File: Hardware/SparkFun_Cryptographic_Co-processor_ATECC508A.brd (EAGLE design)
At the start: 25.4 x 25.4 mm, 41 parts, among them J1 QWIIC, J2 QWIIC, J3 PTH, U1 ATECC508A

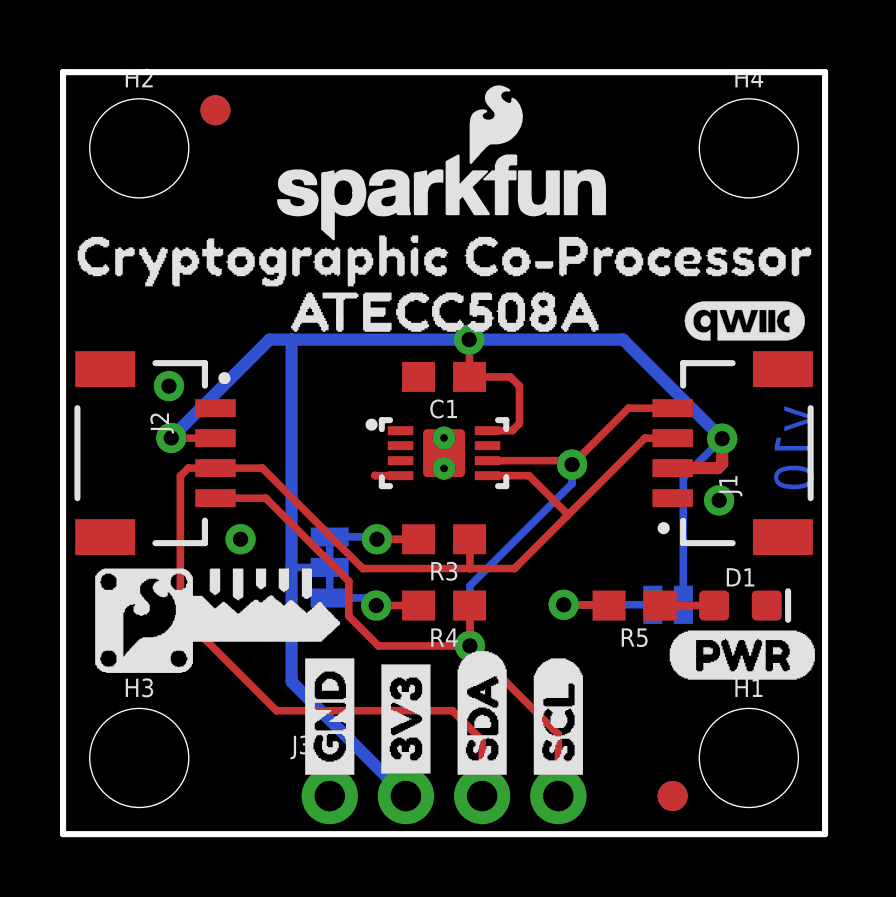
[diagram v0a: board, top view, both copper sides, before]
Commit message: swapped over to official SFE library for IC
added name and value to footprint.
removed local mini library.
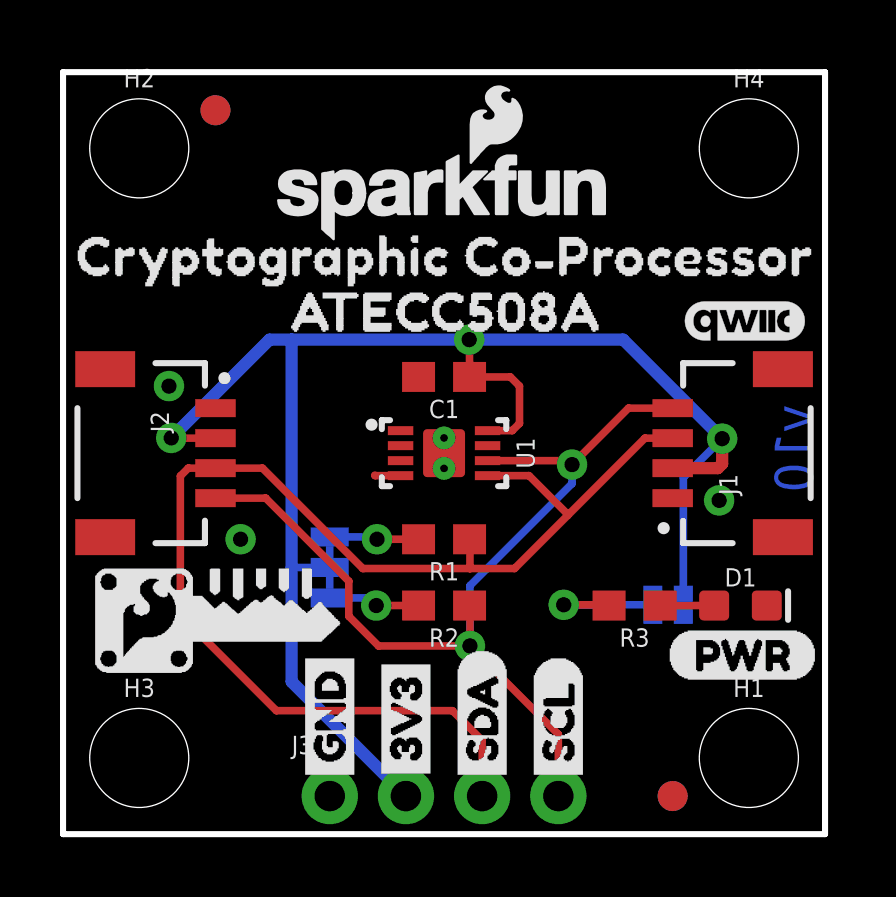
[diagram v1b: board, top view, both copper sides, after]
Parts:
- removed R5: 1k, SparkFun-Resistors:0603
- added R1: 4.7k, SparkFun-Resistors:0603
- R3: value 4.7k -> 1k
- U1: device ATECC508A:UDFN_2X3MM -> SparkFun-IC-Special-Function:UDFN_2X3MM
- moved R3 6.72 mm to (19.1, 7.62)
- renumbered R4 to R2
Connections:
- net N$3: now also R3.1; no longer R5.1
- net N$4: now also R1.2; no longer R3.2
- net N$7: now also R3.2; no longer R5.2
- net SDA: now also R1.1; no longer R3.1
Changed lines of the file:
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@@
 <attribute name="REV" value="" x="-13.97" y="-12.7" size="1.778" layer="27" display="off"/>
 </element>
-<element name="R3" library="SparkFun-Resistors" package="0603" value="4.7k" x="12.7" y="9.8298" smashed="yes" rot="R180">
+<element name="R1" library="SparkFun-Resistors" package="0603" value="4.7k" x="12.7" y="9.8298" smashed="yes" rot="R180">
 <attribute name="NAME" x="12.7" y="9.0678" size="0.6096" layer="25" font="vector" ratio="20" rot="R180" align="bottom-center"/>
 <attribute name="PROD_ID" value="RES-07857" x="12.7" y="9.8298" size="1.778" layer="27" font="vector" ratio="15" rot="R180" display="off"/>
 <attribute name="VALUE" x="12.7" y="10.5918" size="0.6096" layer="27" font="vector" ratio="20" rot="R180" align="top-center"/>
 </element>
-<element name="R4" library="SparkFun-Resistors" package="0603" value="4.7k" x="12.7" y="7.62" smashed="yes" rot="R180">
+<element name="R2" library="SparkFun-Resistors" package="0603" value="4.7k" x="12.7" y="7.62" smashed="yes" rot="R180">
 <attribute name="NAME" x="12.7" y="6.858" size="0.6096" layer="25" font="vector" ratio="20" rot="R180" align="bottom-center"/>
 <attribute name="PROD_ID" value="RES-07857" x="12.7" y="7.62" size="1.778" layer="27" font="vector" ratio="15" rot="R180" display="off"/>
@@
 <attribute name="VALUE" x="22.5806" y="6.985" size="0.6096" layer="27" font="vector" ratio="20" align="top-center"/>
 </element>
-<element name="R5" library="SparkFun-Resistors" package="0603" value="1k" x="19.05" y="7.62" smashed="yes" rot="R180">
+<element name="R3" library="SparkFun-Resistors" package="0603" value="1k" x="19.05" y="7.62" smashed="yes" rot="R180">
 <attribute name="NAME" x="19.05" y="6.858" size="0.6096" layer="25" font="vector" ratio="20" rot="R180" align="bottom-center"/>
 <attribute name="PROD_ID" value="RES-07856" x="19.05" y="7.62" size="1.778" layer="27" font="vector" ratio="15" rot="R180" display="off"/>
@@
 <attribute name="VALUE" x="2.54" y="0.508" size="0.6096" layer="27" font="vector" ratio="20" align="top-center"/>
 </element>
-<element name="U1" library="ATECC508A" package="UDFN_2X3MM" value="ATECC508A" x="12.7" y="12.7" smashed="yes" rot="R270">
-<attribute name="PROD_ID" value="IC-14661" x="12.7" y="12.7" size="1.778" layer="27" rot="R270" display="off"/>
-</element>
 <element name="U$17" library="buzzard_labels (5)" package="CRYPTOGRAPHIC_CO#PROCESSOR0" value="" x="-0.7112" y="19.2786" smashed="yes"/>
 <element name="U$12" library="buzzard_labels (7)" package="ATECC508A0" value="" x="6.4008" y="17.4244" smashed="yes"/>
@@
 <element name="U$15" library="crypto_coprocessor_logo#04#png (1)" package="CRYPTO_COPROCESSOR_LOGO#04#PNG" value="" x="12.7" y="13.97" smashed="yes" rot="MR0"/>
 <element name="U$18" library="crypto_coprocessor_logo#04#png (2)" package="CRYPTO_COPROCESSOR_LOGO#04#PNG" value="" x="5.08" y="7.2136" smashed="yes"/>
+<element name="U1" library="SparkFun-IC-Special-Function" package="UDFN_2X3MM" value="ATECC508A" x="12.7" y="12.7" smashed="yes" rot="R270">
+<attribute name="NAME" x="15.113" y="12.7" size="0.6096" layer="25" font="vector" ratio="20" rot="R270" align="bottom-center"/>
+<attribute name="PROD_ID" value="IC-14661" x="12.7" y="12.7" size="1.778" layer="27" rot="R270" display="off"/>
+<attribute name="VALUE" x="9.906" y="12.7" size="0.6096" layer="27" font="vector" ratio="20" rot="R90" align="bottom-center"/>
+</element>
 </elements>
 <signals>
@@
 <contactref element="C1" pad="2"/>
 <contactref element="D1" pad="C"/>
-<contactref element="U1" pad="4"/>
-<contactref element="U1" pad="P"/>
 <wire x1="12.7" y1="12.7" x2="12.7706" y2="12.6294" width="0.254" layer="1"/>
 <wire x1="12.7" y1="12.7" x2="12.6294" y2="12.6294" width="0.254" layer="1"/>
@@
 <wire x1="10.402" y1="11.95" x2="10.3886" y2="11.9634" width="0.254" layer="1"/>
 <via x="5.9182" y="9.8298" extent="1-16" drill="0.508"/>
+<contactref element="U1" pad="4"/>
+<contactref element="U1" pad="P"/>
 </signal>
 <signal name="SCL">
-<contactref element="R4" pad="1"/>
+<contactref element="R2" pad="1"/>
 <contactref element="J1" pad="4"/>
 <contactref element="J3" pad="4"/>
 <contactref element="J2" pad="4"/>
-<contactref element="U1" pad="6"/>
 <wire x1="20.32" y1="14.2" x2="18.8482" y2="14.2" width="0.254" layer="1"/>
 <wire x1="16.8362" y1="12.45" x2="14.15" y2="12.45" width="0.254" layer="1"/>
@@
 <wire x1="16.9672" y1="12.319" x2="16.9672" y2="11.684" width="0.254" layer="16"/>
 <wire x1="16.9672" y1="11.684" x2="13.5636" y2="8.2804" width="0.254" layer="16"/>
+<contactref element="U1" pad="6"/>
 </signal>
 <signal name="SDA">
-<contactref element="R3" pad="1"/>
+<contactref element="R1" pad="1"/>
 <contactref element="J1" pad="3"/>
 <contactref element="J3" pad="3"/>
 <contactref element="J2" pad="3"/>
-<contactref element="U1" pad="5"/>
 <wire x1="20.32" y1="13.2" x2="19.3976" y2="13.2" width="0.254" layer="1"/>
 <wire x1="5.08" y1="12.2" x2="6.6468" y2="12.2" width="0.254" layer="1"/>
@@
 <wire x1="16.8275" y1="10.6553" x2="16.8275" y2="10.6299" width="0.254" layer="1"/>
 <wire x1="15.5328" y1="11.95" x2="16.8275" y2="10.6553" width="0.254" layer="1"/>
+<contactref element="U1" pad="5"/>
 </signal>
 <signal name="3.3V">
@@
 <contactref element="C1" pad="1"/>
 <contactref element="LED" pad="2"/>
-<contactref element="U1" pad="8"/>
 <wire x1="20.32" y1="12.2" x2="21.8266" y2="12.2" width="0.4064" layer="1"/>
 <wire x1="21.8266" y1="12.2" x2="21.971" y2="12.3444" width="0.4064" layer="1"/>
@@
 <wire x1="7.62" y1="8.89" x2="7.62" y2="16.4846" width="0.4064" layer="16"/>
 <wire x1="8.89" y1="8.89" x2="7.62" y2="8.89" width="0.254" layer="16"/>
+<contactref element="U1" pad="8"/>
 </signal>
 <signal name="N$4">
-<contactref element="R3" pad="2"/>
+<contactref element="R1" pad="2"/>
 <contactref element="I2C" pad="3"/>
 <wire x1="11.85" y1="9.8298" x2="10.4648" y2="9.8298" width="0.254" layer="1"/>
@@
 </signal>
 <signal name="N$5">
-<contactref element="R4" pad="2"/>
+<contactref element="R2" pad="2"/>
 <contactref element="I2C" pad="1"/>
 <wire x1="11.85" y1="7.62" x2="10.4394" y2="7.62" width="0.254" layer="1"/>
@@
 </signal>
 <signal name="N$3">
-<contactref element="R5" pad="1"/>
+<contactref element="R3" pad="1"/>
 <contactref element="D1" pad="A"/>
 <wire x1="21.7036" y1="7.62" x2="19.9" y2="7.62" width="0.254" layer="1"/>
 </signal>
 <signal name="N$7">
-<contactref element="R5" pad="2"/>
+<contactref element="R3" pad="2"/>
 <contactref element="LED" pad="1"/>
 <wire x1="19.6596" y1="7.6454" x2="16.6878" y2="7.6454" width="0.254" layer="16"/>
